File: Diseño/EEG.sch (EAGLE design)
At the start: 42 parts, among them IC1 REF2033AIDDCT, IC2 MCP73831T-2ACI_OT, IC3 LP38692MP-3.3_NOPB, J1 USB3500-30-A-KIT, J2 SJ3-35083A-TR, J3 1769

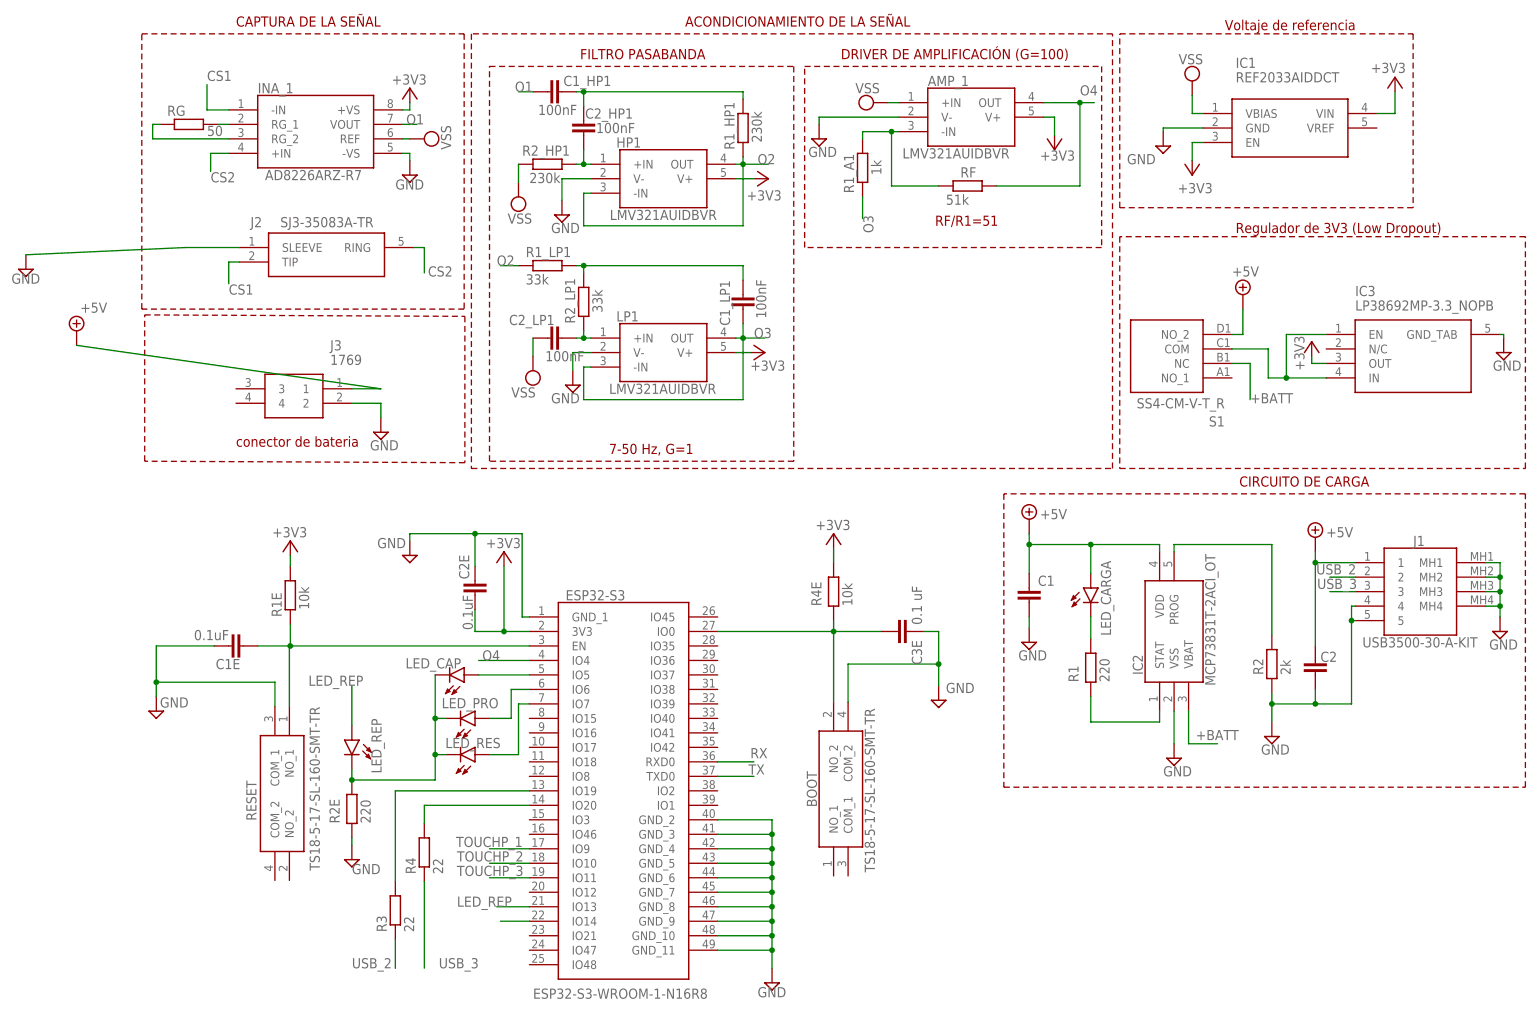
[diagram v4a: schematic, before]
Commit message: añadido oled, componentes nuevos, restio de leds y correcion de pistas
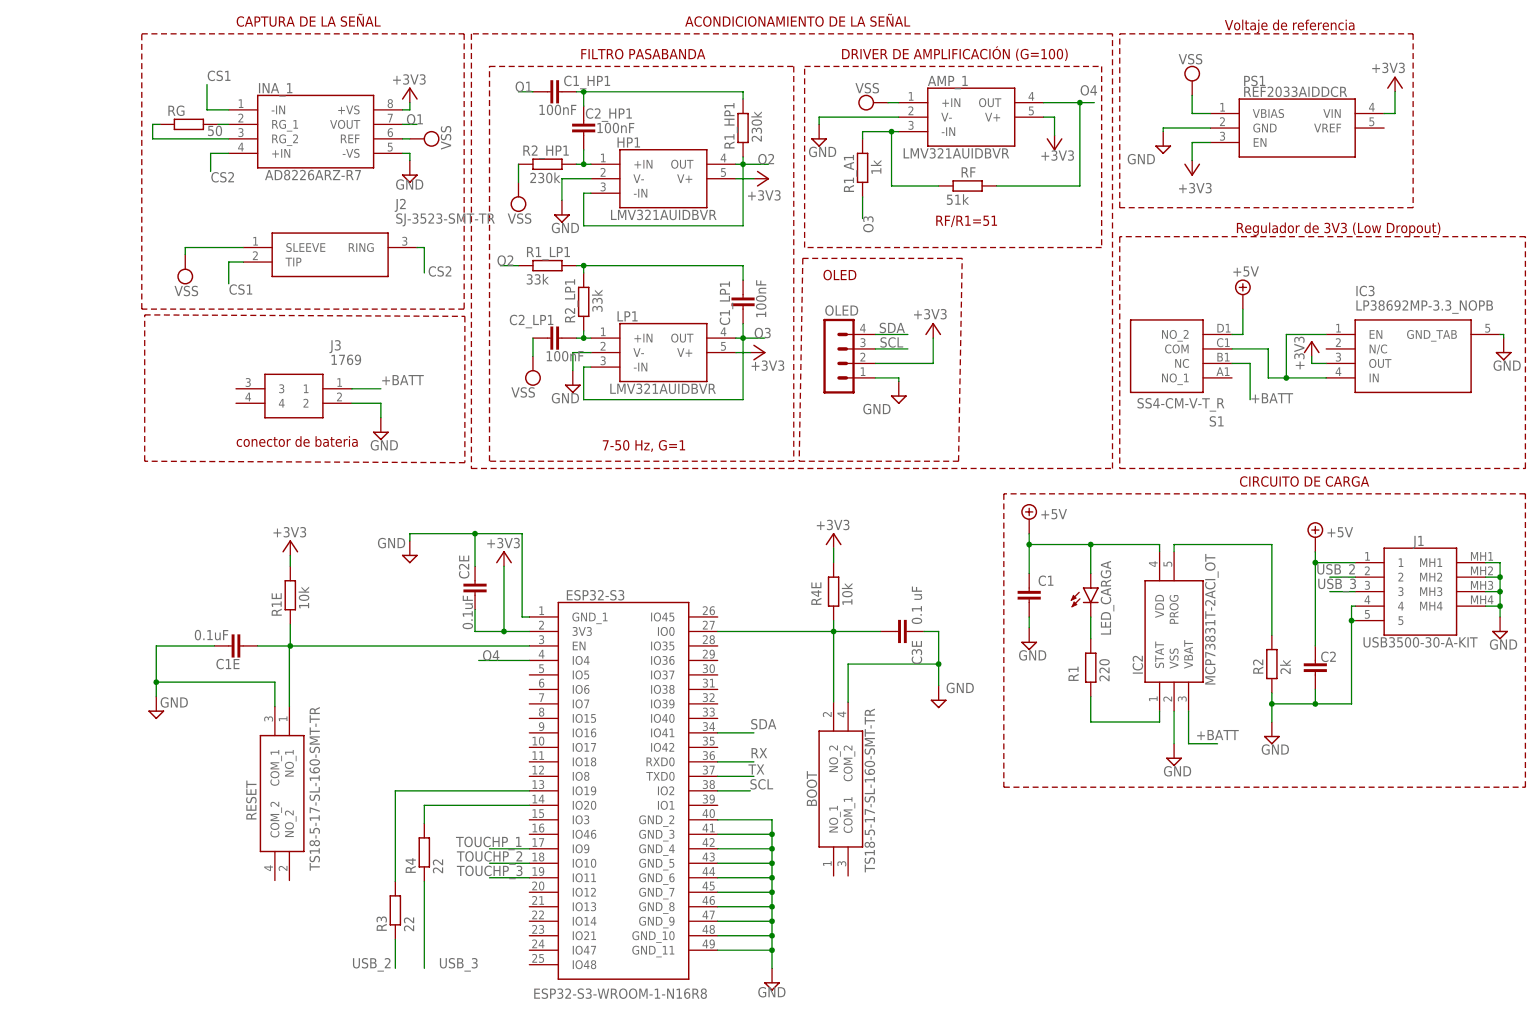
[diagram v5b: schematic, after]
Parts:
- removed IC1: REF2033AIDDCT, REF2033AIDDCT:REF2033AIDDCT
- removed LED_CAP, LED_PRO, LED_REP, LED_RES: (no value), led:LEDCHIPLED_0805
- removed R2E: 220, rcl:R-EU_R0805
- added OLED: (no value), con-lstb:MA04-1
- added PS1: REF2033AIDDCR, REF2033AIDDCR:REF2033AIDDCR
- J2: value SJ3-35083A-TR -> SJ-3523-SMT-TR; device SJ3-35083A-TR:SJ3-35083A-TR -> SJ-3523-SMT-TR:SJ-3523-SMT-TR
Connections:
- removed net +5V1: ESP32-S3.IO14
- removed net LED_REP: ESP32-S3.IO13, LED_REP.A
- removed net N$1: ESP32-S3.IO5, LED_CAP.A
- removed net N$15: LED_CAP.C, LED_PRO.C, LED_REP.C, LED_RES.C, R2E.2
- removed net N$16: ESP32-S3.IO6, LED_PRO.A
- removed net N$17: ESP32-S3.IO7, LED_RES.A
- new net SCL: ESP32-S3.IO2, OLED.3
- new net SDA: ESP32-S3.IO41, OLED.4
- net +3V3: now also OLED.2, PS1.EN, PS1.VIN; no longer IC1.EN, IC1.VIN
- net +5V: no longer J3.1
- net +BATT: now also J3.1
- net GND: now also OLED.1, PS1.GND; no longer IC1.GND, J2.SLEEVE, R2E.1
- net VSS: now also J2.SLEEVE, PS1.VBIAS; no longer IC1.VBIAS
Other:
- note added: "OLED"
- moved on the sheet: J2

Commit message: por fin acabamos esto
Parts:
- C1, C2: value (none) -> 10u
- renumbered AMP_1 to AMP, C1E to C7, C1_HP1 to C3, C1_LP1 to C6, C2E to C8, C2_HP1 to C4, C2_LP1 to C5, C3E to C9, HP1 to HP, INA_1 to INA, LED_CARGA to LED, LP1 to LP, R1E to R11, R1_A1 to R9, R1_HP1 to R6, R1_LP1 to R7, R2_HP1 to R5, R2_LP1 to R8, R4E to R12, RF to R10
